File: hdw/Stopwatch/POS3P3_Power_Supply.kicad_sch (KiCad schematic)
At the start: 13 parts

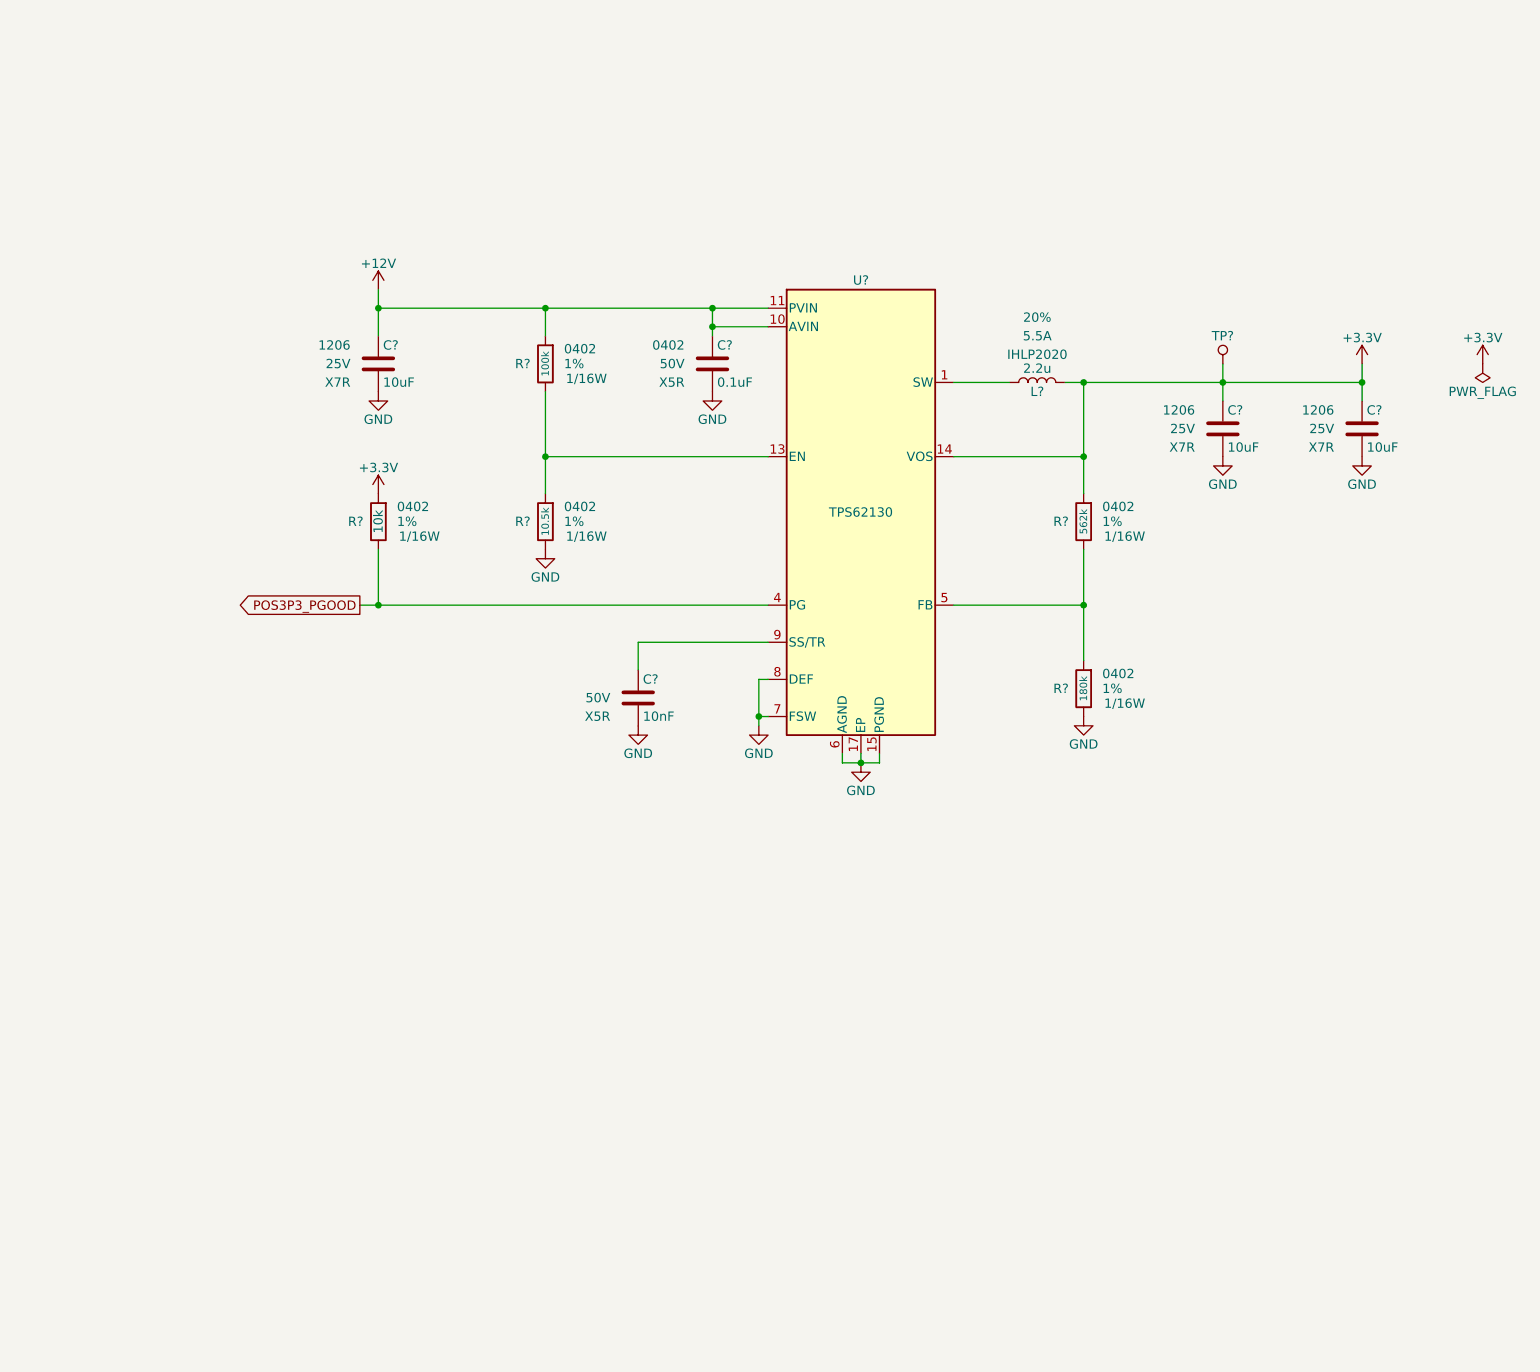
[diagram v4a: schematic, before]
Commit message: added proper power sequencing, discharge
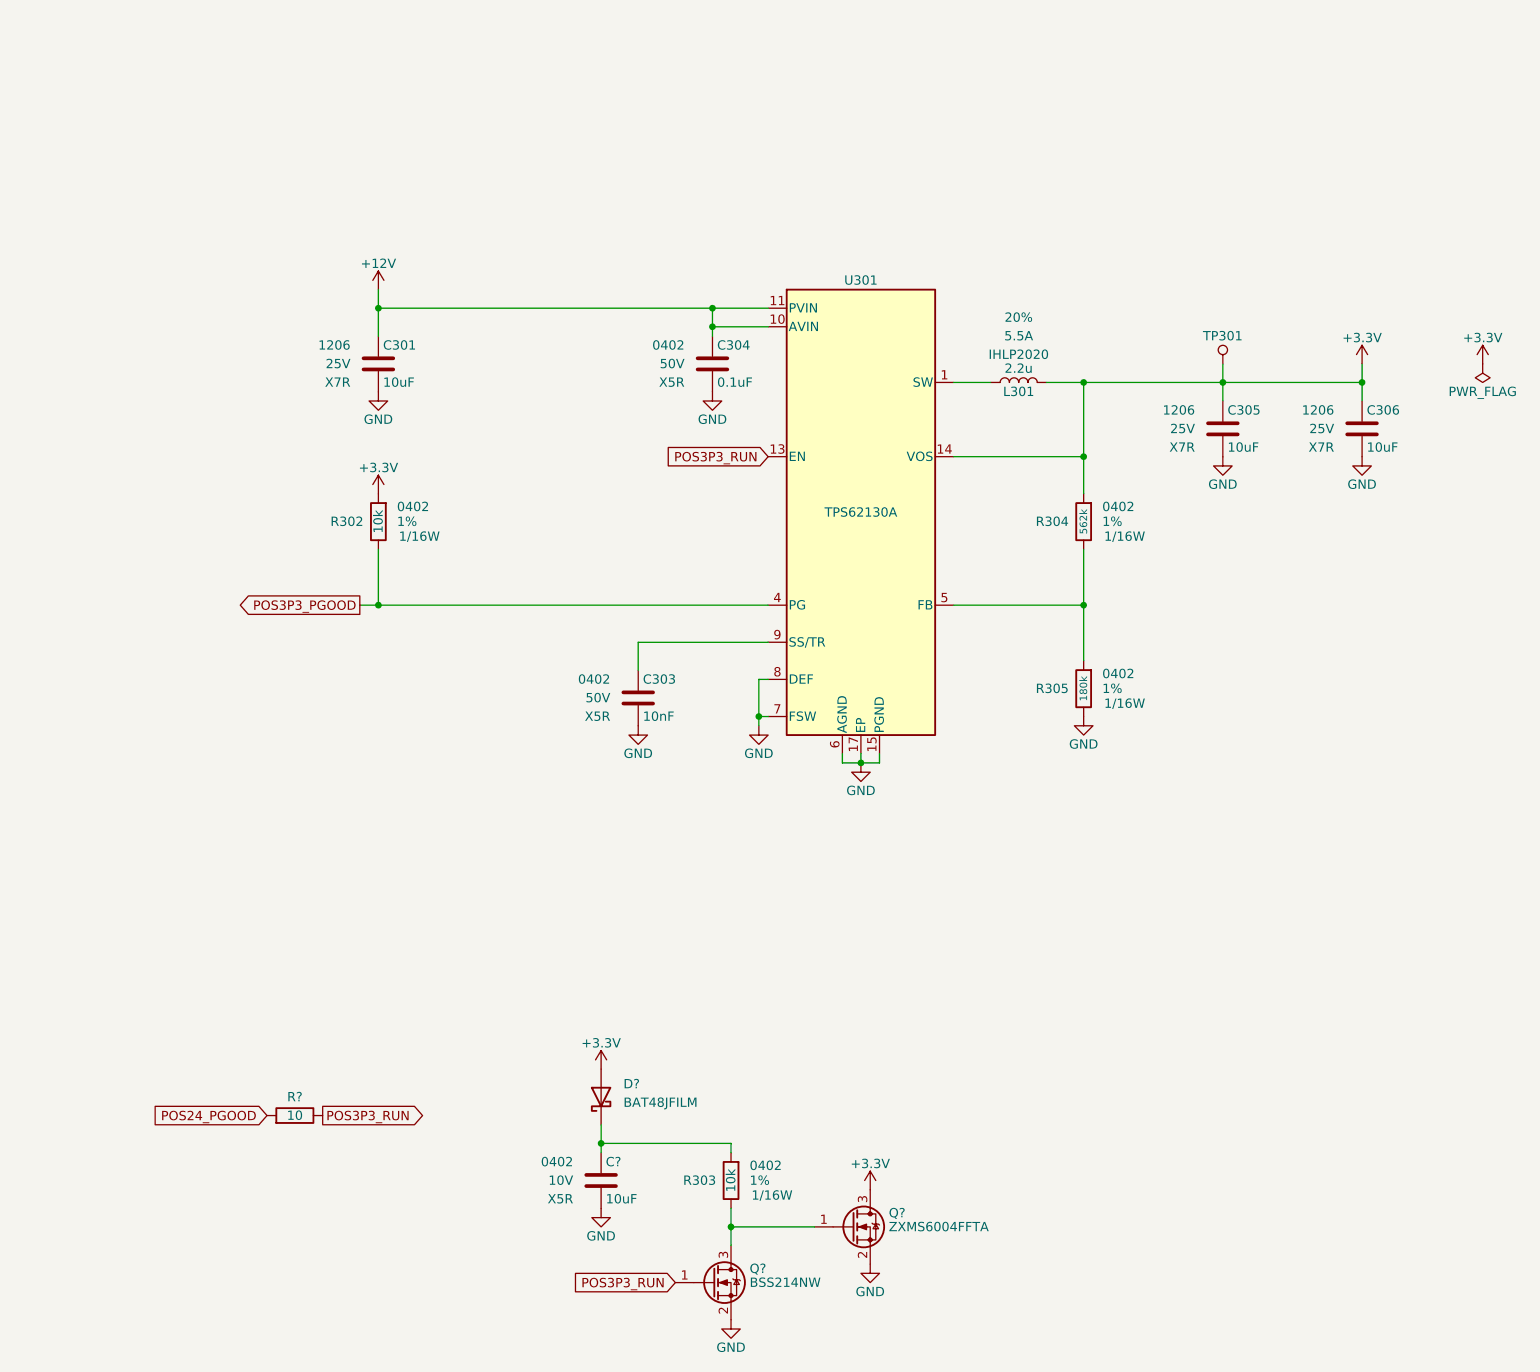
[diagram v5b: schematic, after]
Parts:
- removed R?: 100k, Resistors_SMD:R_0402, symbol Custom_Library:R_Custom
- removed R?: 10.5k, Resistors_SMD:R_0402, symbol Custom_Library:R_Custom
- added C?: 10uF, Capacitors_SMD:C_0402, symbol Custom_Library:C_Custom
- added D?: BAT48JFILM, Diode_SMD:D_SOD-323, symbol Diode:BAT48JFILM
- added Q?: BSS214NW, Package_TO_SOT_SMD:SOT-323_SC-70, symbol Transistor_FET:BSS214NW
- added Q?: ZXMS6004FFTA, Package_TO_SOT_SMD:SOT-23, symbol Custom_Library:ZXMS6004FFTA
- added R303: 10k, Resistors_SMD:R_0402, symbol Custom_Library:R_Custom
- added R?: 10, Resistors_SMD:R_0402, symbol Custom_Library:R_Custom
- C303: renamed from C?; display_footprint (none) -> 0402
- U301: renamed from U?; value TPS62130 -> TPS62130A; Digi-Key PN 296-37878-1-ND -> 296-39446-1-ND
- gave numbers to parts that had none: 9
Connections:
- net GND: now also C?.2, Q?.2 (S), Q?.2 (S)
- net POS3P3_RUN: now reaches U301.13 (EN)
- net POS3P3_RUN: now also Q?.1 (G), R?.2
- new net: Q?.1 (G), Q?.3 (D), R303.2
- new net: C?.1, D?.1 (K), R303.1
- new net +3.3V: D?.2 (A), Q?.3 (D)
- new net POS24_PGOOD: R?.1
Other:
- moved on the sheet: L301

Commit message: lots and lots of routing
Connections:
- net +3V3 is gone; now on net +3.3V: C305.1, C306.1, L301.2, R302.1, R304.1, TP301.1 (TP), U301.14 (VOS)
- net POS24_PGOOD renamed POS12_PGOOD
